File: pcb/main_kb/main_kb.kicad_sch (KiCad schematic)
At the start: 21 parts, among them J1 AVR-ISP-6, J2 TYPE-C-31-M-12, U1 ATMEGA32U4-AU

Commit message: Connected matrix to atmega32u
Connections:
- net row 0: now reaches U1.1 (PE6)
- net SCL: now reaches U1.18 (PD0)
- net SDA: now reaches U1.19 (PD1)
- net col 8: now reaches U1.20 (PD2)
- net col 9: now reaches U1.21 (PD3)
- net col 10: now reaches U1.22 (PD5)
- net col 11: now reaches U1.25 (PD4)
- net col 12: now reaches U1.26 (PD6)
- net col 13: now reaches U1.27 (PD7)
- net col 0: now reaches U1.28 (PB4)
- net col 1: now reaches U1.29 (PB5)
- net col 2: now reaches U1.30 (PB6)
- net col 3: now reaches U1.31 (PC6)
- net col 4: now reaches U1.32 (PC7)
- net col 6: now reaches U1.36 (PF7)
- net col 5: now reaches U1.37 (PF6)
- net row 1: now reaches U1.38 (PF5)
- net row 4: now reaches U1.39 (PF4)
- net row 3: now reaches U1.40 (PF1)
- net row 2: now reaches U1.41 (PF0)
- net col 7: now reaches U1.8 (PB0)
- no-connect marks 6 -> 13
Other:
- moved on the sheet: R1

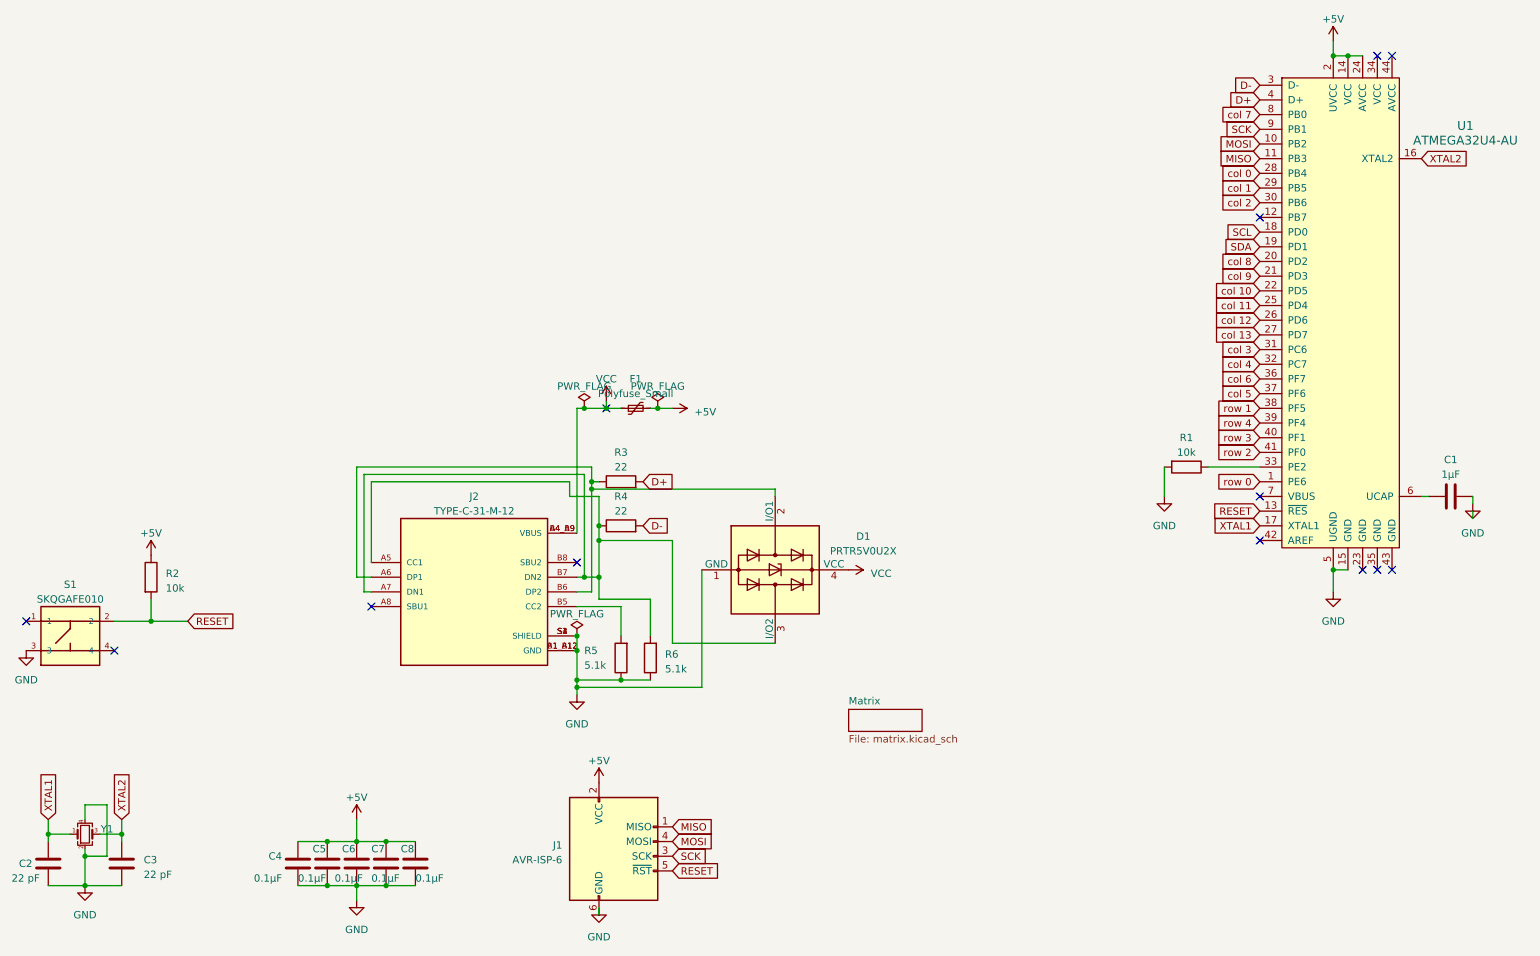
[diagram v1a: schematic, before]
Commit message: Added Pogo Connector
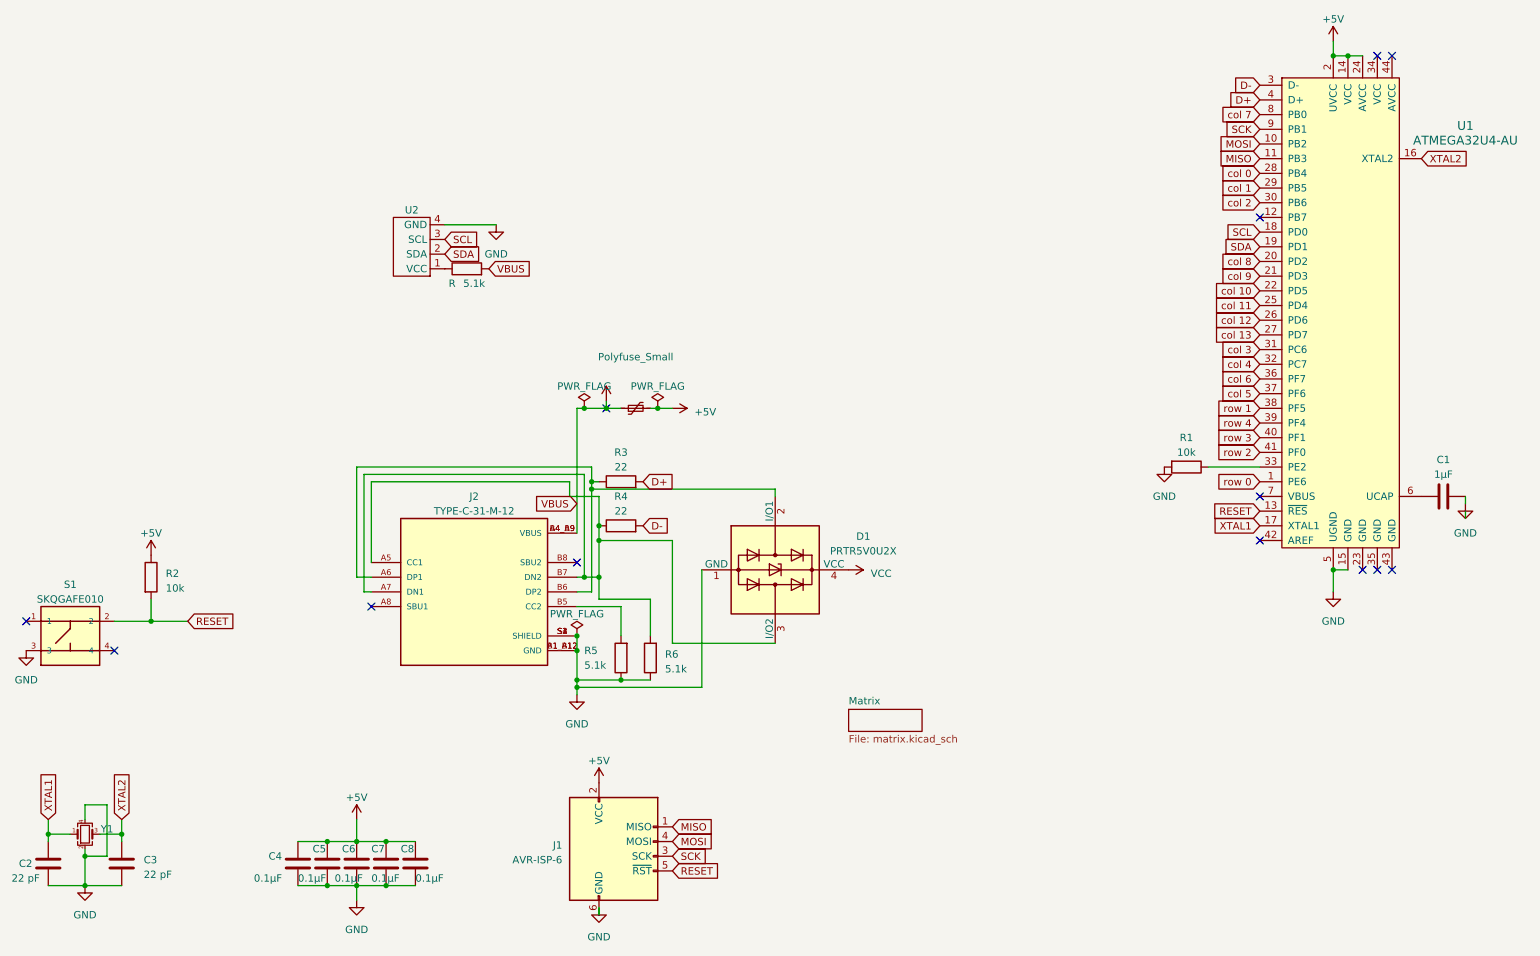
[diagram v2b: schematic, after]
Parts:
- added 5.1k: R, symbol Device:R
- added U2: ~, symbol local:HTP-CON-M411PR-M
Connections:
- net GND: now also U2.4 (GND)
- net SCL: now also U2.3 (SCL)
- net SDA: now also U2.2 (SDA)
- net VCC: now also 5.1k.2
- new net: 5.1k.1, U2.1 (VCC)
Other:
- moved on the sheet: C1
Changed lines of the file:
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@@
+    (stroke (width 0) (type default))
+  )
+  (wire (pts (xy 105.41 66.04) (xy 96.52 66.04))
     (stroke (width 0) (type default))
   )
@@
     (stroke (width 0) (type default))
   )
-  (wire (pts (xy 274.32 113.03) (xy 274.32 114.3))
+  (wire (pts (xy 273.05 113.03) (xy 273.05 114.3))
     (stroke (width 0) (type default))
   )
@@
     (stroke (width 0) (type default))
   )
-  (wire (pts (xy 274.32 115.57) (xy 274.32 116.84))
+  (wire (pts (xy 273.05 115.57) (xy 273.05 116.84))
     (stroke (width 0) (type default))
   )
@@
     (stroke (width 0) (type default))
   )
-  (wire (pts (xy 265.43 113.03) (xy 266.7 113.03))
-    (stroke (width 0) (type default))
-  )
   (wire (pts (xy 34.29 166.37) (xy 38.1 166.37))
     (stroke (width 0) (type default))
@@
   )
   (wire (pts (xy 121.92 107.95) (xy 121.92 110.49))
-    (stroke (width 0) (type default))
-  )
-  (wire (pts (xy 220.98 107.95) (xy 220.98 113.03))
     (stroke (width 0) (type default))
   )
@@
     )
   )
+  (global_label "SDA" (shape input) (at 96.52 71.12 0) (fields_autoplaced)
+    (effects (font (size 1.27 1.27)) (justify left))
+    (property "Intersheetrefs" "${INTERSHEET_REFS}" (at 102.9939 71.12 0)
+      (effects (font (size 1.27 1.27)) (justify left) hide)
+    )
+  )
   (global_label "col 6" (shape input) (at 237.49 92.71 180) (fields_autoplaced)
     (effects (font (size 1.27 1.27)) (justify right))
@@
     )
   )
+  (global_label "VBUS" (shape input) (at 104.14 73.66 0) (fields_autoplaced)
+    (effects (font (size 1.27 1.27)) (justify left))
+    (property "Intersheetrefs" "${INTERSHEET_REFS}" (at 111.9444 73.66 0)
+      (effects (font (size 1.27 1.27)) (justify left) hide)
+    )
+  )
   (global_label "MISO" (shape input) (at 237.49 54.61 180) (fields_autoplaced)
     (effects (font (size 1.27 1.27)) (justify right))
@@
     )
   )
+  (global_label "SCL" (shape input) (at 96.52 68.58 0) (fields_autoplaced)
+    (effects (font (size 1.27 1.27)) (justify left))
+    (property "Intersheetrefs" "${INTERSHEET_REFS}" (at 102.9334 68.58 0)
+      (effects (font (size 1.27 1.27)) (justify left) hide)
+    )
+  )
   (global_label "col 10" (shape input) (at 237.49 77.47 180) (fields_autoplaced)
     (effects (font (size 1.27 1.27)) (justify right))
@@
     (property "Intersheetrefs" "${INTERSHEET_REFS}" (at 273.8391 54.61 0)
       (effects (font (size 1.27 1.27)) (justify left) hide)
+    )
+  )
+  (global_label "VBUS" (shape input) (at 119.38 114.3 180) (fields_autoplaced)
+    (effects (font (size 1.27 1.27)) (justify right))
+    (property "Intersheetrefs" "${INTERSHEET_REFS}" (at 111.5756 114.3 0)
+      (effects (font (size 1.27 1.27)) (justify right) hide)
     )
   )
@@
   )
   (symbol (lib_id "Device:Polyfuse_Small") (at 129.54 97.79 90) (unit 1)
-    (in_bom yes) (on_board yes) (dnp no) (fields_autoplaced)
+    (in_bom yes) (on_board yes) (dnp no)
     (property "Reference" "F1" (at 129.54 92.71 90)
-      (effects (font (size 1.27 1.27)))
-    )
-    (property "Value" "Polyfuse_Small" (at 129.54 95.25 90)
+      (effects (font (size 1.27 1.27)) hide)
+    )
+    (property "Value" "Polyfuse_Small" (at 129.54 88.9 90)
       (effects (font (size 1.27 1.27)))
     )
@@
         (path "/baab57f8-6b9c-4e76-bad2-b70e6a890058"
           (reference "R2") (unit 1)
+        )
+      )
+    )
+  )
+  (symbol (lib_id "power:GND") (at 105.41 66.04 0) (unit 1)
+    (in_bom yes) (on_board yes) (dnp no) (fields_autoplaced)
+    (property "Reference" "#PWR016" (at 105.41 72.39 0)
+      (effects (font (size 1.27 1.27)) hide)
+    )
+    (property "Value" "GND" (at 105.41 71.12 0)
+      (effects (font (size 1.27 1.27)))
+    )
+    (property "Footprint" "" (at 105.41 66.04 0)
+      (effects (font (size 1.27 1.27)) hide)
+    )
+    (property "Datasheet" "" (at 105.41 66.04 0)
+      (effects (font (size 1.27 1.27)) hide)
+    )
+    (pin "1")
+    (instances
+      (project "main_kb"
+        (path "/baab57f8-6b9c-4e76-bad2-b70e6a890058"
+          (reference "#PWR016") (unit 1)
         )
       )
@@
     )
   )
+  (symbol (lib_id "Device:R") (at 100.33 73.66 90) (unit 1)
+    (in_bom yes) (on_board yes) (dnp no)
+    (property "Reference" "5.1k" (at 101.6 76.2 90)
+      (effects (font (size 1.27 1.27)))
+    )
+    (property "Value" "R" (at 97.79 76.2 90)
+      (effects (font (size 1.27 1.27)))
+    )
+    (property "Footprint" "" (at 100.33 75.438 90)
+      (effects (font (size 1.27 1.27)) hide)
+    )
+    (property "Datasheet" "~" (at 100.33 73.66 0)
+      (effects (font (size 1.27 1.27)) hide)
+    )
+    (pin "1")
+    (pin "2")
+    (instances
+      (project "main_kb"
+        (path "/baab57f8-6b9c-4e76-bad2-b70e6a890058"
+          (reference "5.1k") (unit 1)
+        )
+      )
+    )
+  )
   (symbol (lib_id "Device:R") (at 132.08 140.97 180) (unit 1)
     (in_bom yes) (on_board yes) (dnp no) (fields_autoplaced)
@@
     )
     (property "Value" "VCC" (at 124.46 92.71 0)
-      (effects (font (size 1.27 1.27)))
+      (effects (font (size 1.27 1.27)) hide)
     )
     (property "Footprint" "" (at 124.46 96.52 0)
@@
     )
   )
-  (symbol (lib_id "Device:C") (at 270.51 113.03 90) (unit 1)
-    (in_bom yes) (on_board yes) (dnp no) (fields_autoplaced)
-    (property "Reference" "C1" (at 270.51 106.68 90)
-      (effects (font (size 1.27 1.27)))
-    )
-    (property "Value" "1µF" (at 270.51 109.22 90)
-      (effects (font (size 1.27 1.27)))
-    )
-    (property "Footprint" "" (at 274.32 112.0648 0)
-      (effects (font (size 1.27 1.27)) hide)
-    )
-    (property "Datasheet" "~" (at 270.51 113.03 0)
+  (symbol (lib_id "Device:C") (at 269.24 113.03 90) (unit 1)
+    (in_bom yes) (on_board yes) (dnp no) (fields_autoplaced)
+    (property "Reference" "C1" (at 269.24 106.68 90)
+      (effects (font (size 1.27 1.27)))
+    )
+    (property "Value" "1µF" (at 269.24 109.22 90)
+      (effects (font (size 1.27 1.27)))
+    )
+    (property "Footprint" "" (at 273.05 112.0648 0)
+      (effects (font (size 1.27 1.27)) hide)
+    )
+    (property "Datasheet" "~" (at 269.24 113.03 0)
       (effects (font (size 1.27 1.27)) hide)
     )
@@
     )
   )
-  (symbol (lib_id "power:GND") (at 220.98 113.03 0) (unit 1)
-    (in_bom yes) (on_board yes) (dnp no) (fields_autoplaced)
-    (property "Reference" "#PWR03" (at 220.98 119.38 0)
-      (effects (font (size 1.27 1.27)) hide)
-    )
-    (property "Value" "GND" (at 220.98 118.11 0)
-      (effects (font (size 1.27 1.27)))
-    )
-    (property "Footprint" "" (at 220.98 113.03 0)
-      (effects (font (size 1.27 1.27)) hide)
-    )
-    (property "Datasheet" "" (at 220.98 113.03 0)
+  (symbol (lib_id "local:HTP-CON-M411PR-M") (at 91.44 71.12 180) (unit 1)
+    (in_bom yes) (on_board yes) (dnp no) (fields_autoplaced)
+    (property "Reference" "U2" (at 90.805 63.5 0)
+      (effects (font (size 1.27 1.27)))
+    )
+    (property "Value" "~" (at 91.44 71.12 0)
+      (effects (font (size 1.27 1.27)))
+    )
+    (property "Footprint" "" (at 91.44 71.12 0)
+      (effects (font (size 1.27 1.27)) hide)
+    )
+    (property "Datasheet" "" (at 91.44 71.12 0)
+      (effects (font (size 1.27 1.27)) hide)
+    )
+    (pin "1")
+    (pin "2")
+    (pin "3")
+    (pin "4")
+    (instances
+      (project "main_kb"
+        (path "/baab57f8-6b9c-4e76-bad2-b70e6a890058"
+          (reference "U2") (unit 1)
+        )
+      )
+    )
+  )
+  (symbol (lib_id "power:GND") (at 220.98 107.95 0) (unit 1)
+    (in_bom yes) (on_board yes) (dnp no) (fields_autoplaced)
+    (property "Reference" "#PWR03" (at 220.98 114.3 0)
+      (effects (font (size 1.27 1.27)) hide)
+    )
+    (property "Value" "GND" (at 220.98 113.03 0)
+      (effects (font (size 1.27 1.27)))
+    )
+    (property "Footprint" "" (at 220.98 107.95 0)
+      (effects (font (size 1.27 1.27)) hide)
+    )
+    (property "Datasheet" "" (at 220.98 107.95 0)
       (effects (font (size 1.27 1.27)) hide)
     )
@@
     )
   )
-  (symbol (lib_id "power:GND") (at 274.32 114.3 0) (unit 1)
-    (in_bom yes) (on_board yes) (dnp no) (fields_autoplaced)
-    (property "Reference" "#PWR04" (at 274.32 120.65 0)
-      (effects (font (size 1.27 1.27)) hide)
-    )
-    (property "Value" "GND" (at 274.32 119.38 0)
-      (effects (font (size 1.27 1.27)))
-    )
-    (property "Footprint" "" (at 274.32 114.3 0)
-      (effects (font (size 1.27 1.27)) hide)
-    )
-    (property "Datasheet" "" (at 274.32 114.3 0)
-      (effects (font (size 1.27 1.27)) hide)
-    )
+  (symbol (lib_id "power:GND") (at 273.05 114.3 0) (unit 1)
+    (in_bom yes) (on_board yes) (dnp no) (fields_autoplaced)
+    (property "Reference" "#PWR04" (at 273.05 120.65 0)
+      (effects (font (size 1.27 1.27)) hide)
+    )
+    (property "Value" "GND" (at 273.05 119.38 0)
+      (effects (font (size 1.27 1.27)))
+    )
+    (property "Footprint" "" (at 273.05 114.3 0)
+      (effects (font (size 1.27 1.27)) hide)
+    )
+    (property "Datasheet" "" (at 273.05 114.3 0)
+      (effects (font (size 1.27 1.27)) hide)
+    )
